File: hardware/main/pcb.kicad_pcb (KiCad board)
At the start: 2 copper layers, 55 x 55 mm, 24 parts, among them J1 Conn_01x02_Socket, J2 Conn_01x02_Socket

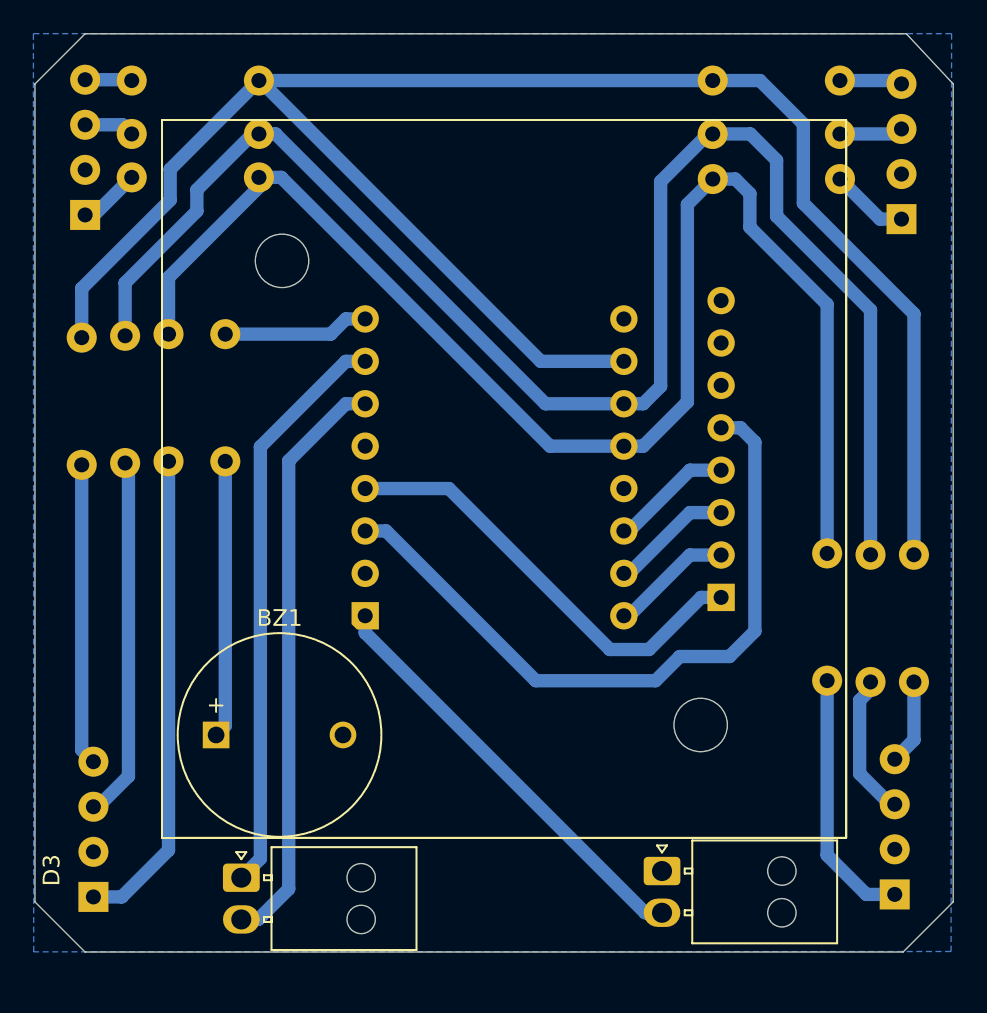
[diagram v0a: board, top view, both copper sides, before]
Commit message: add trasistors to for led diode board
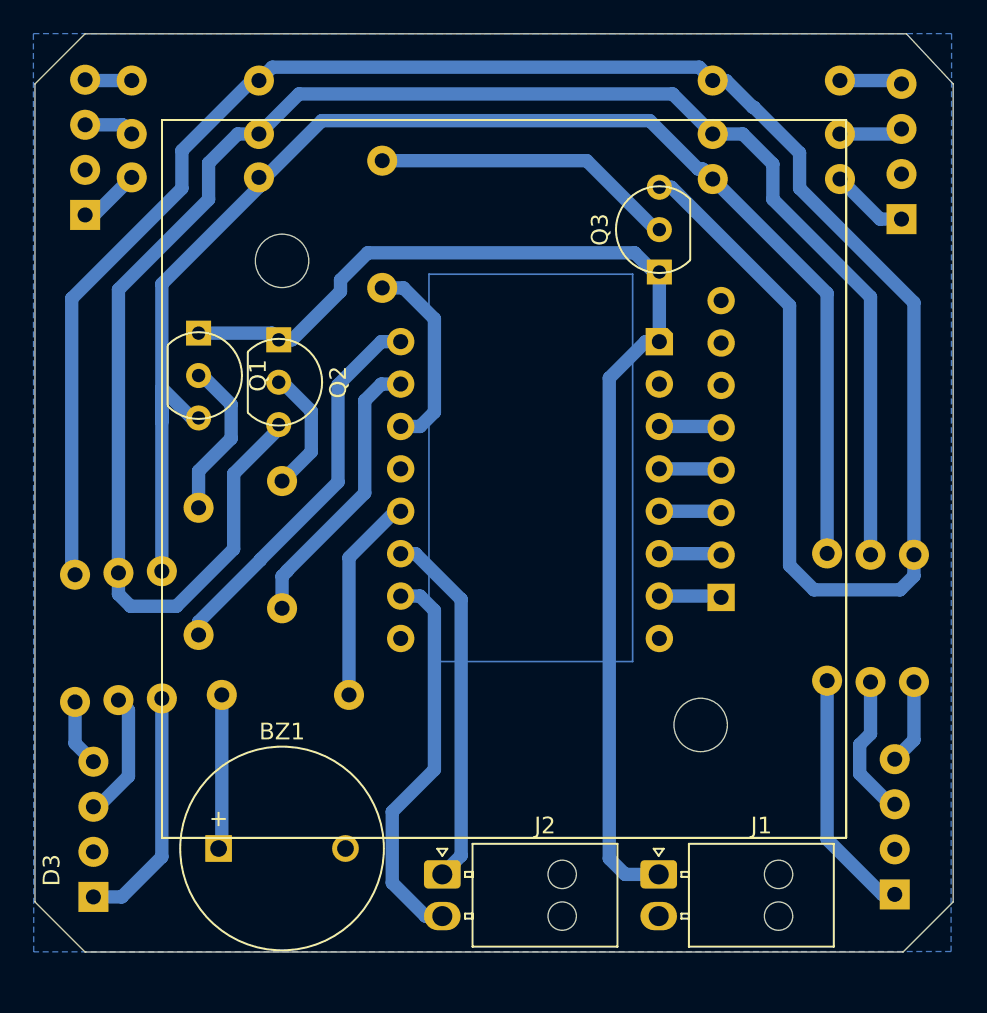
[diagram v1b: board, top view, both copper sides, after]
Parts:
- added Q1: BC547, Package_TO_SOT_THT:TO-92_Inline, F.Cu at (109.8, 59.2)
- added Q2: BC547, Package_TO_SOT_THT:TO-92_Inline, F.Cu at (114.6, 59.6)
- added Q3: BC547, Package_TO_SOT_THT:TO-92_Inline, F.Cu at (137.4, 53.0)
- added R14: 1000, Resistor_THT:CNC_Ready_R_Axial_DIN0204_L3.6mm_D1.6mm_P7.62mm_Horizontal, F.Cu at (109.8, 76.0)
- added R15: 1000, Resistor_THT:CNC_Ready_R_Axial_DIN0204_L3.6mm_D1.6mm_P7.62mm_Horizontal, F.Cu at (114.8, 74.4)
- added R16: 1000, Resistor_THT:CNC_Ready_R_Axial_DIN0204_L3.6mm_D1.6mm_P7.62mm_Horizontal, F.Cu at (120.8, 55.2)
- J1: value Conn_01x02_Socket -> POWER
- J2: value Conn_01x02_Socket -> OUTPUT
- moved R13 22.8 mm to (118.8, 79.6), turned to 180 degrees
- moved R7 14.2 mm to (102.4, 72.4)
- moved R8 14.2 mm to (105.0, 72.3)
- moved R9 14.2 mm to (107.6, 72.2)
- moved J2 12.0 mm to (124.4, 90.3)
- moved BZ1 6.80 mm to (111.0, 88.8)
- moved U1 4.57 mm to (129.8, 68.6), turned to 180 degrees
- moved J1 0.28 mm to (137.4, 90.3)
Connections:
- J1 pad 1: GND -> +5V
- J1 pad 2: Net-(J1-Pin_2) -> GND
- R1 pad 1: /R -> Net-(Q1-E)
- R10 pad 1: /B -> Net-(Q3-E)
- R11 pad 1: /G -> Net-(Q2-E)
- R12 pad 1: /R -> Net-(Q1-E)
- R13 pad 1: Net-(U1-GPIO0) -> Net-(U1-GPIO9/SCL)
- R2 pad 1: /G -> Net-(Q2-E)
- R3 pad 1: /B -> Net-(Q3-E)
- R4 pad 1: /B -> Net-(Q3-E)
- R5 pad 1: /G -> Net-(Q2-E)
- R6 pad 1: /R -> Net-(Q1-E)
- R7 pad 1: /B -> Net-(Q3-E)
- R8 pad 1: /G -> Net-(Q2-E)
- R9 pad 1: /R -> Net-(Q1-E)
- U1 pad 1: Net-(J1-Pin_2) -> +5V
- U1 pad 10: Net-(U1-GPIO6/MOSI) -> /G
- U1 pad 11: Net-(U1-GPIO7/SS) -> /B
- U1 pad 13: /R -> Net-(U1-GPIO9/SCL)
- U1 pad 14: /G -> Net-(J2-Pin_1)
- U1 pad 15: /B -> Net-(J2-Pin_2)
- U1 pad 5: unconnected-(U1-GPIO3-Pad5) -> Net-(U1-GPIO3)
- U1 pad 6: Net-(J2-Pin_2) -> Net-(U1-GPIO2)
- U1 pad 7: Net-(J2-Pin_1) -> Net-(U1-GPIO1)
- U1 pad 8: Net-(U1-GPIO0) -> unconnected-(U1-GPIO0-Pad8)
- U1 pad 9: Net-(U1-GPIO5/MISO) -> /R
- U2 pad 5: Net-(U1-GPIO4/SCK) -> Net-(U1-GPIO1)
- U2 pad 6: Net-(U1-GPIO5/MISO) -> Net-(U1-GPIO2)
- U2 pad 7: Net-(U1-GPIO6/MOSI) -> Net-(U1-GPIO3)
- U2 pad 8: Net-(U1-GPIO7/SS) -> Net-(U1-GPIO4/SCK)
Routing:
- net Net-(Q3-E): track 0.00 -> 132.3 mm
- net Net-(Q2-E): track 0.00 -> 108.3 mm
- net /B: track 110.9 -> 12.2 mm
- net Net-(Q1-E): track 0.00 -> 86.1 mm
- net /G: track 93.8 -> 17.1 mm
- net +5V: track 0.00 -> 71.3 mm
- net /R: track 85.1 -> 23.6 mm
- net Net-(U1-3V3): track 42.0 -> 4.05 mm
- net Net-(J1-Pin_2): track 25.7 -> 0.00 mm
- net Net-(U1-GPIO4/SCK): track 26.6 -> 3.73 mm
- net Net-(Q3-B): track 0.00 -> 18.3 mm
- net Net-(D3-RA): track 28.9 -> 14.6 mm
- net Net-(D3-GA): track 21.7 -> 7.67 mm
- net Net-(D3-BA): track 18.1 -> 4.04 mm
- net Net-(J2-Pin_1): track 34.7 -> 21.7 mm
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
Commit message: update the pcb design
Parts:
- moved R16 22.7 mm to (118.8, 77.8)
- moved Q3 21.4 mm to (117.0, 59.4), turned to -90 degrees
- moved BZ1 8.40 mm to (119.2, 87.0), turned to 180 degrees
- moved R13 7.20 mm to (126.0, 79.2), turned to -90 degrees
- moved R15 3.42 mm to (114.4, 77.8)
- moved Q1 2.43 mm to (107.4, 59.6)
- moved Q2 2.40 mm to (112.2, 59.6)
- moved R14 2.01 mm to (110.0, 78.0)
- moved D1 0.25 mm to (103.0, 51.1)
- moved J2 0.15 mm to (124.4, 90.2)
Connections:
- R13 pad 1: Net-(U1-GPIO9/SCL) -> unconnected-(R13-Pad1)
- U1 pad 10: /G -> Net-(J2-Pin_1)
- U1 pad 11: /B -> unconnected-(U1-GPIO7/SS-Pad11)
- U1 pad 13: Net-(U1-GPIO9/SCL) -> /R
- U1 pad 14: Net-(J2-Pin_1) -> /G
- U1 pad 15: Net-(J2-Pin_2) -> /B
- U1 pad 9: /R -> Net-(J2-Pin_2)
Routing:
- net (no net): track 0.00 -> 18.4 mm
- net Net-(J2-Pin_2): track 23.6 -> 41.1 mm
- net Net-(J2-Pin_1): track 21.7 -> 34.7 mm
- net Net-(U1-GPIO9/SCL): track 12.5 -> 0.00 mm
- net Net-(Q3-E): track 132.3 -> 122.3 mm
- net Net-(Q3-B): track 18.3 -> 10.4 mm
- net /G: track 17.1 -> 10.3 mm
- net /B: track 12.2 -> 6.10 mm
- net +5V: track 71.3 -> 67.8 mm
- net Net-(BZ1-+): track 9.28 -> 6.88 mm
- net Net-(Q2-B): track 7.58 -> 9.76 mm
- net /R: track 23.6 -> 25.7 mm
- net Net-(D1-RA): track 3.72 -> 4.37 mm

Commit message: update the board
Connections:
- R13 pad 1: unconnected-(R13-Pad1) -> Net-(U1-GPIO7/SS)
- U1 pad 11: unconnected-(U1-GPIO7/SS-Pad11) -> Net-(U1-GPIO7/SS)
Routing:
- net Net-(U1-GPIO7/SS): track 0.00 -> 18.4 mm
- net (no net): track 18.4 -> 0.00 mm
- net /R: track 25.7 -> 26.5 mm
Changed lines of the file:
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@@
 	(net 35 "Net-(J2-Pin_1)")
 	(net 36 "Net-(J2-Pin_2)")
-	(net 37 "unconnected-(R13-Pad1)")
-	(net 38 "unconnected-(U1-GPIO7{slash}SS-Pad11)")
+	(net 37 "Net-(U1-GPIO7{slash}SS)")
 	(footprint "Resistor_THT:CNC_Ready_R_Axial_DIN0204_L3.6mm_D1.6mm_P7.62mm_Horizontal"
 		(layer "F.Cu")
@@
 			(layers "*.Cu" "*.Mask")
 			(remove_unused_layers no)
-			(net 37 "unconnected-(R13-Pad1)")
+			(net 37 "Net-(U1-GPIO7{slash}SS)")
 			(pintype "passive")
 		)
@@
 			(layers "*.Cu" "*.Mask")
 			(remove_unused_layers no)
-			(net 38 "unconnected-(U1-GPIO7{slash}SS-Pad11)")
+			(net 37 "Net-(U1-GPIO7{slash}SS)")
 			(pinfunction "GPIO7/SS")
 			(pintype "bidirectional")
@@
 	)
 	(segment
-		(start 126 79.19)
-		(end 126 66.454345)
-		(width 0.8)
-		(layer "B.Cu")
-		(net 0)
-	)
-	(segment
-		(start 123.065655 63.52)
-		(end 121.906 63.52)
-		(width 0.8)
-		(layer "B.Cu")
-		(net 0)
-	)
-	(segment
-		(start 121.906 63.52)
-		(end 121.587874 63.52)
-		(width 0.8)
-		(layer "B.Cu")
-		(net 0)
-	)
-	(segment
-		(start 126 66.454345)
-		(end 123.065655 63.52)
-		(width 0.8)
-		(layer "B.Cu")
-		(net 0)
-	)
-	(segment
 		(start 105.495 45.7)
 		(end 105.795 46)
@@
 	)
 	(segment
-		(start 121.906 68.6)
-		(end 122.224126 68.6)
+		(start 111.901 79.911)
+		(end 110 78.01)
 		(width 0.8)
 		(layer "B.Cu")
@@
 	)
 	(segment
-		(start 123.927 70.302874)
-		(end 123.927 77.057126)
+		(start 123.927 78.473)
+		(end 122.489 79.911)
 		(width 0.8)
 		(layer "B.Cu")
@@
 	)
 	(segment
-		(start 123.927 77.057126)
-		(end 121.073126 79.911)
+		(start 121.906 68.6)
+		(end 122.224126 68.6)
 		(width 0.8)
 		(layer "B.Cu")
@@
 	)
 	(segment
-		(start 122.224126 68.6)
-		(end 123.927 70.302874)
+		(start 123.927 70.302874)
+		(end 123.927 78.473)
 		(width 0.8)
 		(layer "B.Cu")
@@
 	)
 	(segment
-		(start 111.901 79.911)
-		(end 110 78.01)
+		(start 122.489 79.911)
+		(end 111.901 79.911)
 		(width 0.8)
 		(layer "B.Cu")
@@
 	)
 	(segment
-		(start 121.073126 79.911)
-		(end 111.901 79.911)
+		(start 122.224126 68.6)
+		(end 123.927 70.302874)
 		(width 0.8)
 		(layer "B.Cu")
@@
 		(net 36)
 	)
+	(segment
+		(start 126 79.19)
+		(end 126 66.454345)
+		(width 0.8)
+		(layer "B.Cu")
+		(net 37)
+	)
+	(segment
+		(start 123.065655 63.52)
+		(end 121.906 63.52)
+		(width 0.8)
+		(layer "B.Cu")
+		(net 37)
+	)
+	(segment
+		(start 121.906 63.52)
+		(end 121.587874 63.52)
+		(width 0.8)
+		(layer "B.Cu")
+		(net 37)
+	)
+	(segment
+		(start 126 66.454345)
+		(end 123.065655 63.52)
+		(width 0.8)
+		(layer "B.Cu")
+		(net 37)
+	)
 	(zone

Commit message: add gerber file
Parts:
- moved R13 3.43 mm to (127.2, 82.4), turned to 180 degrees
- moved BZ1 1.63 mm to (118.9, 88.6)
- moved J1 0.90 mm to (138.3, 90.3)
- moved J2 0.90 mm to (125.3, 90.5)
- moved R1 0.10 mm to (113.4, 48.7)
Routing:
- net Net-(U1-GPIO7/SS): track 18.4 -> 22.1 mm
- net Net-(Q2-E): track 108.5 -> 106.0 mm
- net Net-(Q1-E): track 85.9 -> 83.6 mm
- net Net-(J2-Pin_2): track 41.1 -> 42.7 mm
- net Net-(J2-Pin_1): track 34.7 -> 36.2 mm
- net Net-(Q3-E): track 122.3 -> 121.7 mm

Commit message: Add labels (#40)
* add tag emular tool

* fix the buzzer

* add lables
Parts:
- Q1, Q2, Q3: value BC547 -> BC337
- U1: value ~ -> ESP32 C3 supper mini
- moved REF** 0.16 mm to (140.0, 81.5)
- moved REF** 0.10 mm to (114.8, 53.7)
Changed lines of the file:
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@@
 		)
 		(property "Value" "100"
-			(at -2.48 0 0)
-			(layer "F.SilkS")
-			(hide yes)
+			(at 3.805 0 0)
+			(layer "B.SilkS")
 			(effects
 				(font
@@
 					(thickness 0.15)
 				)
+				(justify mirror)
 			)
 		)
@@
 			)
 		)
-		(property "Value" "BC547"
-			(at 1.27 2.79 90)
-			(layer "F.Fab")
+		(property "Value" "BC337"
+			(at 1.7 -1.5 90)
+			(layer "B.SilkS")
 			(effects
 				(font
@@
 					(thickness 0.15)
 				)
+				(justify mirror)
 			)
 		)
@@
 		)
 		(property "Value" "150"
-			(at -2.48 0 0)
-			(layer "F.SilkS")
-			(hide yes)
+			(at 3.715 0 0)
+			(layer "B.SilkS")
 			(effects
 				(font
@@
 					(thickness 0.15)
 				)
+				(justify mirror)
 			)
 		)
@@
 		)
 		(property "Value" "100"
-			(at -2.48 0 90)
-			(layer "F.SilkS")
-			(hide yes)
+			(at 4.095 -0.05 90)
+			(layer "B.SilkS")
 			(effects
 				(font
@@
 					(thickness 0.15)
 				)
+				(justify mirror)
 			)
 		)
@@
 		)
 		(property "Value" "100"
-			(at -2.48 0 0)
-			(layer "F.SilkS")
-			(hide yes)
+			(at 3.715 0 0)
+			(layer "B.SilkS")
 			(effects
 				(font
@@
 					(thickness 0.15)
 				)
+				(justify mirror)
 			)
 		)
@@
 		)
 		(property "Value" "150"
-			(at -2.48 0 90)
-			(layer "F.SilkS")
-			(hide yes)
+			(at 4.095 -0.05 90)
+			(layer "B.SilkS")
 			(effects
 				(font
@@
 					(thickness 0.15)
 				)
+				(justify mirror)
 			)
 		)
@@
 		)
 		(property "Value" "100"
-			(at -2.48 0 0)
-			(layer "F.SilkS")
-			(hide yes)
+			(at 3.715 0 0)
+			(layer "B.SilkS")
 			(effects
 				(font
@@
 					(thickness 0.15)
 				)
+				(justify mirror)
 			)
 		)
@@
 		)
 		(property "Value" "100"
-			(at -2.48 0 90)
-			(layer "F.SilkS")
-			(hide yes)
+			(at 4.095 -0.05 90)
+			(layer "B.SilkS")
 			(effects
 				(font
@@
 					(thickness 0.15)
 				)
+				(justify mirror)
 			)
 		)
@@
 		)
 		(property "Value" "100"
-			(at -2.48 0 90)
-			(layer "F.SilkS")
-			(hide yes)
+			(at 4.1 0 90)
+			(layer "B.SilkS")
 			(effects
 				(font
@@
 					(thickness 0.15)
 				)
+				(justify mirror)
 			)
 		)
@@
 			)
 		)
-		(property "Value" "BC547"
-			(at 1.27 2.79 90)
-			(layer "F.Fab")
+		(property "Value" "BC337"
+			(at 1.4 -1.4 90)
+			(layer "B.SilkS")
 			(effects
 				(font
@@
 					(thickness 0.15)
 				)
+				(justify mirror)
 			)
 		)
@@
 		)
 		(property "Value" "100"
-			(at -2.48 0 90)
-			(layer "F.SilkS")
-			(hide yes)
+			(at 4.21 0 90)
+			(layer "B.SilkS")
 			(effects
 				(font
@@
 					(thickness 0.15)
 				)
+				(justify mirror)
 			)
 		)
@@
 			)
 		)
-		(property "Value" "BC547"
-			(at 1.27 2.79 90)
-			(layer "F.Fab")
+		(property "Value" "BC337"
+			(at 1.6 -1.5 90)
+			(layer "B.SilkS")
 			(effects
 				(font
@@
 					(thickness 0.15)
 				)
+				(justify mirror)
 			)
 		)
@@
 		)
 		(property "Value" "150"
-			(at -2.48 0 0)
-			(layer "F.SilkS")
-			(hide yes)
+			(at 4.2 0 0)
+			(layer "B.SilkS")
 			(effects
 				(font
@@
 					(thickness 0.15)
 				)
+				(justify mirror)
 			)
 		)
@@
 		(property "Reference" "BZ1"
 			(at 3.8 -7 0)
-			(layer "F.SilkS")
+			(layer "B.SilkS")
+			(hide yes)
 			(effects
 				(font
@@
 					(thickness 0.15)
 				)
+				(justify mirror)
 			)
 		)
 		(property "Value" "Buzzer"
-			(at 3.8 7 0)
-			(layer "F.Fab")
+			(at 4.4 -0.1 90)
+			(layer "B.SilkS")
 			(effects
 				(font
@@
 					(thickness 0.15)
 				)
+				(justify mirror)
 			)
 		)
@@
 		(pad "1" thru_hole rect
 			(at 0 0 180)
-			(size 1.6 1.6)
-			(drill 1)
+			(size 3 2.2)
+			(drill oval 2 1)
 			(layers "*.Cu" "*.Mask")
 			(remove_unused_layers no)
@@
 			(pintype "passive")
 		)
-		(pad "2" thru_hole circle
+		(pad "2" thru_hole oval
 			(at 7.6 0 180)
-			(size 1.6 1.6)
-			(drill 1)
+			(size 3 2.2)
+			(drill oval 2 1)
 			(layers "*.Cu" "*.Mask")
 			(remove_unused_layers no)
@@
 		)
 		(property "Value" "100"
-			(at -2.48 0 0)
-			(layer "F.SilkS")
-			(hide yes)
+			(at 3.905 0 0)
+			(layer "B.SilkS")
 			(effects
 				(font
@@
 					(thickness 0.15)
 				)
+				(justify mirror)
 			)
 		)
@@
 		)
 		(property "Value" "150"
-			(at -2.48 0 90)
-			(layer "F.SilkS")
-			(hide yes)
+			(at 4.31 0 90)
+			(layer "B.SilkS")
 			(effects
 				(font
@@
 					(thickness 0.15)
 				)
+				(justify mirror)
 			)
 		)
@@
 	(footprint "MountingHole:MountingHole_3.2mm_M3_DIN965"
 		(layer "B.Cu")
-		(at 139.875 81.4 180)
+		(at 140 81.5 180)
 		(descr "Mounting Hole 3.2mm, M3, no annular, generated by kicad-footprint-generator mountinghole.py")
 		(tags "mountinghole M3 DIN965")
@@
 	(footprint "MountingHole:MountingHole_3.2mm_M3_DIN965"
 		(layer "B.Cu")
-		(at 114.8 53.6 180)
+		(at 114.8 53.7 180)
 		(descr "Mounting Hole 3.2mm, M3, no annular, generated by kicad-footprint-generator mountinghole.py")
 		(tags "mountinghole M3 DIN965")
@@
 			)
 		)
-		(property "Value" "~"
-			(at 0 -1 0)
+		(property "Value" "ESP32 C3 supper mini"
+			(at 0 -1 90)
 			(unlocked yes)
-			(layer "B.Fab")
+			(layer "B.SilkS")
 			(effects
 				(font

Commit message: add mark for 1k resistor
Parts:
- R14, R15, R16: value 1000 -> 1K
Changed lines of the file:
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@@
 			)
 		)
-		(property "Value" "1000"
-			(at -2.48 0 90)
-			(layer "F.SilkS")
-			(hide yes)
-			(effects
-				(font
-					(size 1 1)
-					(thickness 0.15)
-				)
+		(property "Value" "1K"
+			(at 4.11 0 90)
+			(layer "B.SilkS")
+			(effects
+				(font
+					(size 1 1)
+					(thickness 0.15)
+				)
+				(justify mirror)
 			)
 		)
@@
 			)
 		)
-		(property "Value" "1000"
-			(at -2.48 0 90)
-			(layer "F.SilkS")
-			(hide yes)
-			(effects
-				(font
-					(size 1 1)
-					(thickness 0.15)
-				)
+		(property "Value" "1K"
+			(at 4.11 0 90)
+			(layer "B.SilkS")
+			(effects
+				(font
+					(size 1 1)
+					(thickness 0.15)
+				)
+				(justify mirror)
 			)
 		)
@@
 			)
 		)
-		(property "Value" "1000"
-			(at -2.48 0 90)
-			(layer "F.SilkS")
-			(hide yes)
-			(effects
-				(font
-					(size 1 1)
-					(thickness 0.15)
-				)
-			)
-		)
+		(property "Value" "1K"
+			(at 4.11 0 90)
+			(layer "B.SilkS")
+			(effects
+				(font
+					(size 1 1)
+					(thickness 0.15)
+				)
+				(justify mirror)
+			)
+		)

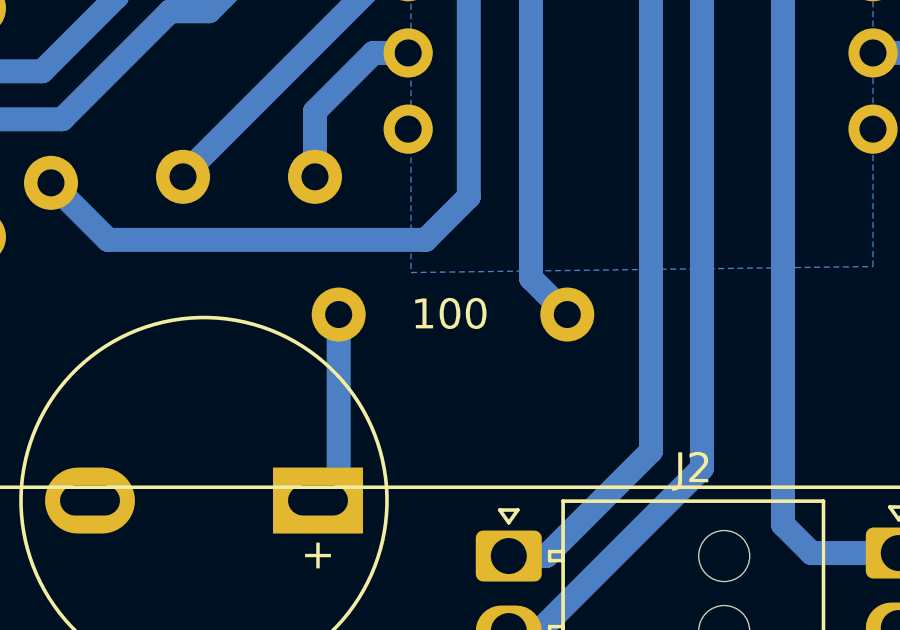
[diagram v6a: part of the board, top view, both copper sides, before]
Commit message: add labels
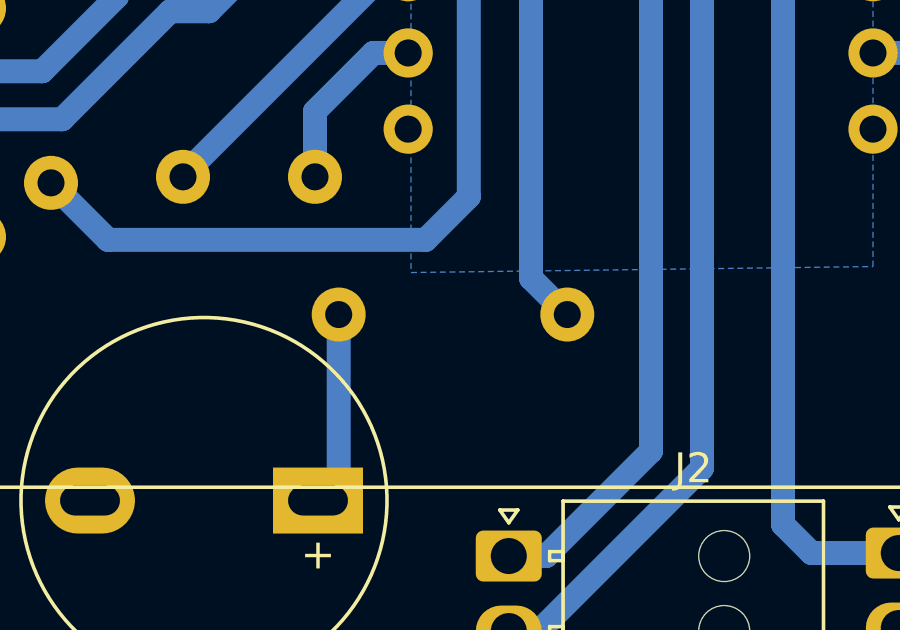
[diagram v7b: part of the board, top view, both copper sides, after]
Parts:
- R13: value 100 -> 1K
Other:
- board text added: "+"
- board text added: "+5V"
- board text added: "GND"
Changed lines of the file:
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@@
 			)
 		)
-		(property "Value" "100"
+		(property "Value" "1K"
 			(at 3.91 0 0)
-			(layer "F.SilkS")
-			(effects
-				(font
-					(size 1 1)
-					(thickness 0.15)
-				)
+			(layer "B.SilkS")
+			(effects
+				(font
+					(size 1 1)
+					(thickness 0.15)
+				)
+				(justify mirror)
 			)
 		)
@@
 		(layer "Edge.Cuts")
 	)
+	(gr_text "+"
+		(at 121 89.3 0)
+		(layer "B.SilkS")
+		(effects
+			(font
+				(size 1 1)
+				(thickness 0.15)
+			)
+			(justify left bottom)
+		)
+	)
+	(gr_text "+5V"
+		(at 143 91.1 0)
+		(layer "B.SilkS")
+		(effects
+			(font
+				(size 1 1)
+				(thickness 0.15)
+			)
+			(justify left bottom mirror)
+		)
+	)
+	(gr_text "GND"
+		(at 142.7 93.6 0)
+		(layer "B.SilkS")
+		(effects
+			(font
+				(size 1 1)
+				(thickness 0.15)
+			)
+			(justify left bottom mirror)
+		)
+	)
 	(segment

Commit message: update pcb
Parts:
- removed J1: POWER, Connector_Molex:Molex_Nano-Fit_105313-xx02_1x02_P2.50mm_Horizontal
- removed J2: OUTPUT, Connector_Molex:Molex_Nano-Fit_105313-xx02_1x02_P2.50mm_Horizontal
- added J3: Conn_01x03_Socket, Connector_PinSocket_2.54mm:PinSocket_1x03_P2.54mm_Vertical_with_holes, F.Cu at (136.6, 88.1)
- Q1, Q2, Q3: value BC337 -> BC547
- R13: value 1K -> 100
- R14, R15, R16: value 1K -> 1000
- U1: value ESP32 C3 supper mini -> ~
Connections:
- U1 pad 10: Net-(J2-Pin_1) -> unconnected-(U1-GPIO6/MOSI-Pad10)
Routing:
- net Net-(J2-Pin_1): track 36.2 -> 0.00 mm
- net +5V: track 67.8 -> 66.6 mm
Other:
- board text added: "Prismo 1.0.0-alpha.1 Kyiv, Ukraine HackerSpace NU31"
- board text added: "RKGB"
- board text added: "SUCCESS"
- board text added: "Слава Україні"
